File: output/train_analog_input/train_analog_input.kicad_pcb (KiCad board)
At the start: 2 copper layers, 65 x 40 mm, 29 parts, among them J1 Screw_Terminal_2P, J2 Screw_Terminal_2P, J3 Screw_Terminal_2P, J4 Screw_Terminal_2P, J5 PinHeader_1x04, U1 ADS1115

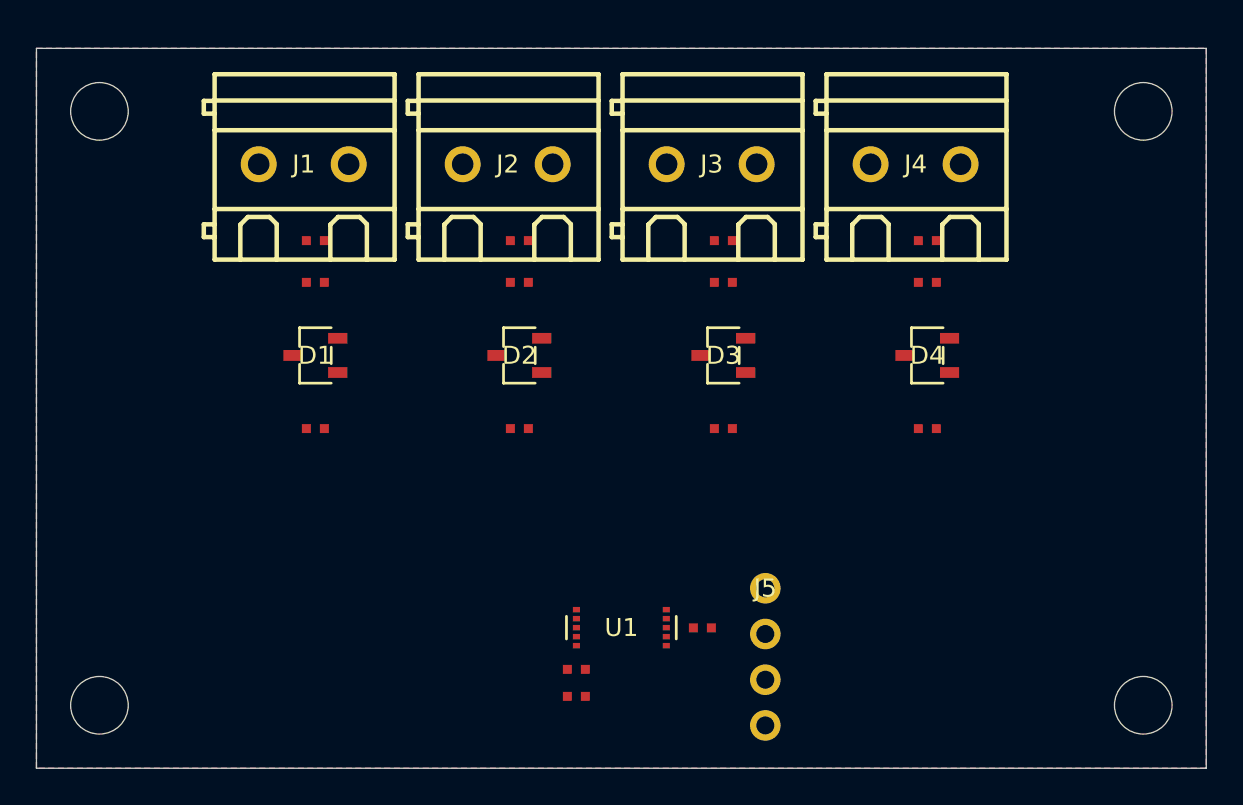
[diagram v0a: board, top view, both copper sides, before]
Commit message: pcb-review(analog): shift ADC components 2mm toward top edge
Moved J1-J4 and all ADC channel components (R1-R8, C2-C5, D1-D4)
2mm closer to the top board edge. Connector Edge score 0.871->0.940.
Score 0.9832 -> 0.9844. Grade A, 0 violations.

Co-Authored-By: Claude Opus 4.6 (1M context) <noreply@anthropic.com>
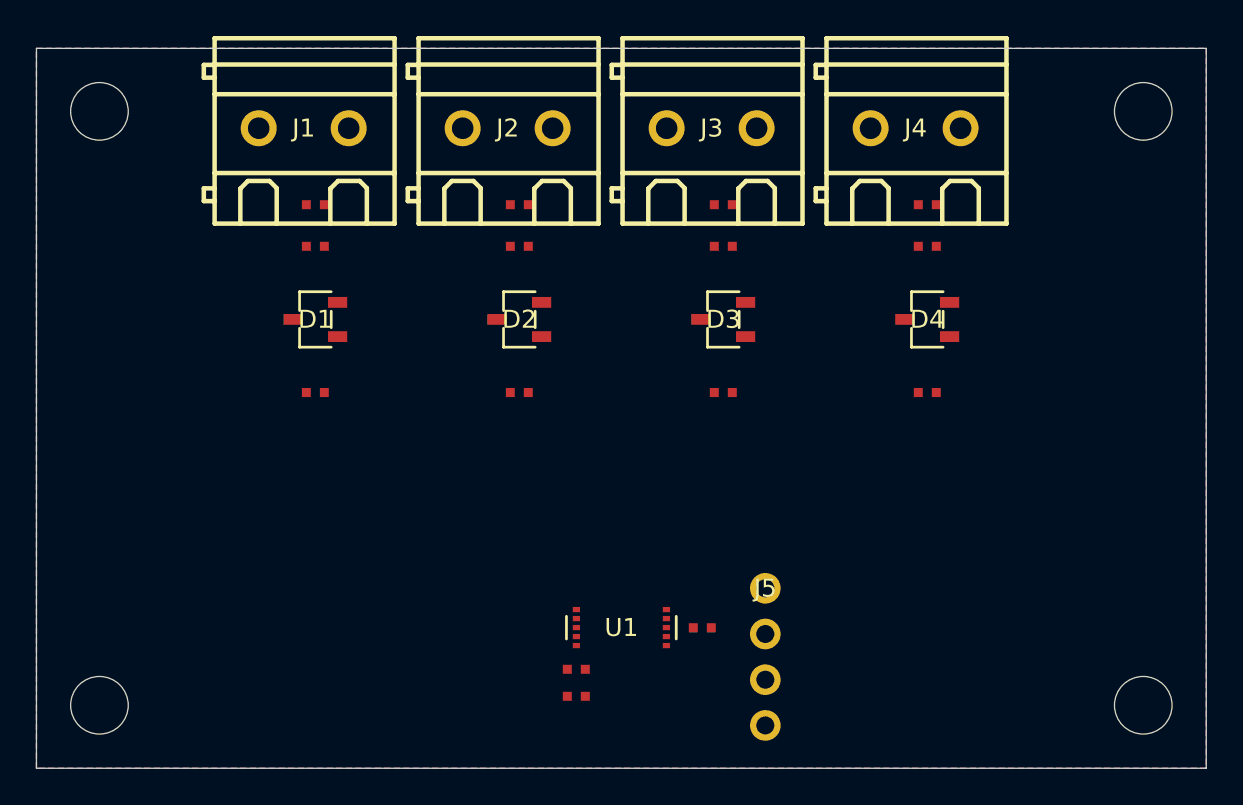
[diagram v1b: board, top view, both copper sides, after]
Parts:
- moved C2 2.00 mm to (15.5, 11.0)
- moved C3 2.00 mm to (26.8, 11.0)
- moved C4 2.00 mm to (38.2, 11.0)
- moved C5 2.00 mm to (49.5, 11.0)
- moved D1 2.00 mm to (15.5, 15.1)
- moved D2 2.00 mm to (26.8, 15.1)
- moved D3 2.00 mm to (38.2, 15.1)
- moved D4 2.00 mm to (49.5, 15.1)
- moved J1 2.00 mm to (14.8, 4.44)
- moved J2 2.00 mm to (26.2, 4.44)
- moved J3 2.00 mm to (37.5, 4.44)
- moved J4 2.00 mm to (48.9, 4.44)
- moved R1 2.00 mm to (15.5, 8.69)
- moved R2 2.00 mm to (15.5, 19.1)
- moved R3 2.00 mm to (26.8, 8.69)
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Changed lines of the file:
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@@
   (footprint "Resistor_SMD:R_0402_1005Metric"
     (layer "F.Cu")
-    (at 15.5 10.6875 0.0)
+    (at 15.5 8.6875 0.0)
     (attr smd)
     (property "Reference" "R1"
@@
   (footprint "Resistor_SMD:R_0402_1005Metric"
     (layer "F.Cu")
-    (at 15.5 21.125 0.0)
+    (at 15.5 19.125 0.0)
     (attr smd)
     (property "Reference" "R2"
@@
   (footprint "easyeda2kicad:SOT-23-3_L2.9-W1.6-P1.90-LS2.8-BR"
     (layer "F.Cu")
-    (at 15.5 17.0625 0.0)
+    (at 15.5 15.0625 0.0)
     (attr smd)
     (property "Reference" "D1"
@@
   (footprint "Capacitor_SMD:C_0402_1005Metric"
     (layer "F.Cu")
-    (at 15.5 13.0 0.0)
+    (at 15.5 11.0 0.0)
     (attr smd)
     (property "Reference" "C2"
@@
   (footprint "easyeda2kicad:CONN-TH_2P-P5.00_WJ128V-5.0-2P"
     (layer "F.Cu")
-    (at 14.85 6.4375 0.0)
+    (at 14.85 4.4375 0.0)
     (attr through_hole)
     (property "Reference" "J1"
@@
   (footprint "Resistor_SMD:R_0402_1005Metric"
     (layer "F.Cu")
-    (at 26.8333 10.6875 0.0)
+    (at 26.8333 8.6875 0.0)
     (attr smd)
     (property "Reference" "R3"
@@
   (footprint "Resistor_SMD:R_0402_1005Metric"
     (layer "F.Cu")
-    (at 26.8333 21.125 0.0)
+    (at 26.8333 19.125 0.0)
     (attr smd)
     (property "Reference" "R4"
@@
   (footprint "easyeda2kicad:SOT-23-3_L2.9-W1.6-P1.90-LS2.8-BR"
     (layer "F.Cu")
-    (at 26.8333 17.0625 0.0)
+    (at 26.8333 15.0625 0.0)
     (attr smd)
     (property "Reference" "D2"
@@
   (footprint "Capacitor_SMD:C_0402_1005Metric"
     (layer "F.Cu")
-    (at 26.8333 13.0 0.0)
+    (at 26.8333 11.0 0.0)
     (attr smd)
     (property "Reference" "C3"
@@
   (footprint "easyeda2kicad:CONN-TH_2P-P5.00_WJ128V-5.0-2P"
     (layer "F.Cu")
-    (at 26.1833 6.4375 0.0)
+    (at 26.1833 4.4375 0.0)
     (attr through_hole)
     (property "Reference" "J2"
@@
   (footprint "Resistor_SMD:R_0402_1005Metric"
     (layer "F.Cu")
-    (at 38.1667 10.6875 0.0)
+    (at 38.1667 8.6875 0.0)
     (attr smd)
     (property "Reference" "R5"
@@
   (footprint "Resistor_SMD:R_0402_1005Metric"
     (layer "F.Cu")
-    (at 38.1667 21.125 0.0)
+    (at 38.1667 19.125 0.0)
     (attr smd)
     (property "Reference" "R6"
@@
   (footprint "easyeda2kicad:SOT-23-3_L2.9-W1.6-P1.90-LS2.8-BR"
     (layer "F.Cu")
-    (at 38.1667 17.0625 0.0)
+    (at 38.1667 15.0625 0.0)
     (attr smd)
     (property "Reference" "D3"
@@
   (footprint "Capacitor_SMD:C_0402_1005Metric"
     (layer "F.Cu")
-    (at 38.1667 13.0 0.0)
+    (at 38.1667 11.0 0.0)
     (attr smd)
     (property "Reference" "C4"
@@
   (footprint "easyeda2kicad:CONN-TH_2P-P5.00_WJ128V-5.0-2P"
     (layer "F.Cu")
-    (at 37.5167 6.4375 0.0)
+    (at 37.5167 4.4375 0.0)
     (attr through_hole)
     (property "Reference" "J3"
@@
   (footprint "Resistor_SMD:R_0402_1005Metric"
     (layer "F.Cu")
-    (at 49.5 10.6875 0.0)
+    (at 49.5 8.6875 0.0)
     (attr smd)
     (property "Reference" "R7"
@@
   (footprint "Resistor_SMD:R_0402_1005Metric"
     (layer "F.Cu")
-    (at 49.5 21.125 0.0)
+    (at 49.5 19.125 0.0)
     (attr smd)
     (property "Reference" "R8"
@@
   (footprint "easyeda2kicad:SOT-23-3_L2.9-W1.6-P1.90-LS2.8-BR"
     (layer "F.Cu")
-    (at 49.5 17.0625 0.0)
+    (at 49.5 15.0625 0.0)
     (attr smd)
     (property "Reference" "D4"
@@
   (footprint "Capacitor_SMD:C_0402_1005Metric"
     (layer "F.Cu")
-    (at 49.5 13.0 0.0)
+    (at 49.5 11.0 0.0)
     (attr smd)
     (property "Reference" "C5"
@@
   (footprint "easyeda2kicad:CONN-TH_2P-P5.00_WJ128V-5.0-2P"
     (layer "F.Cu")
-    (at 48.85 6.4375 0.0)
+    (at 48.85 4.4375 0.0)
     (attr through_hole)
     (property "Reference" "J4"

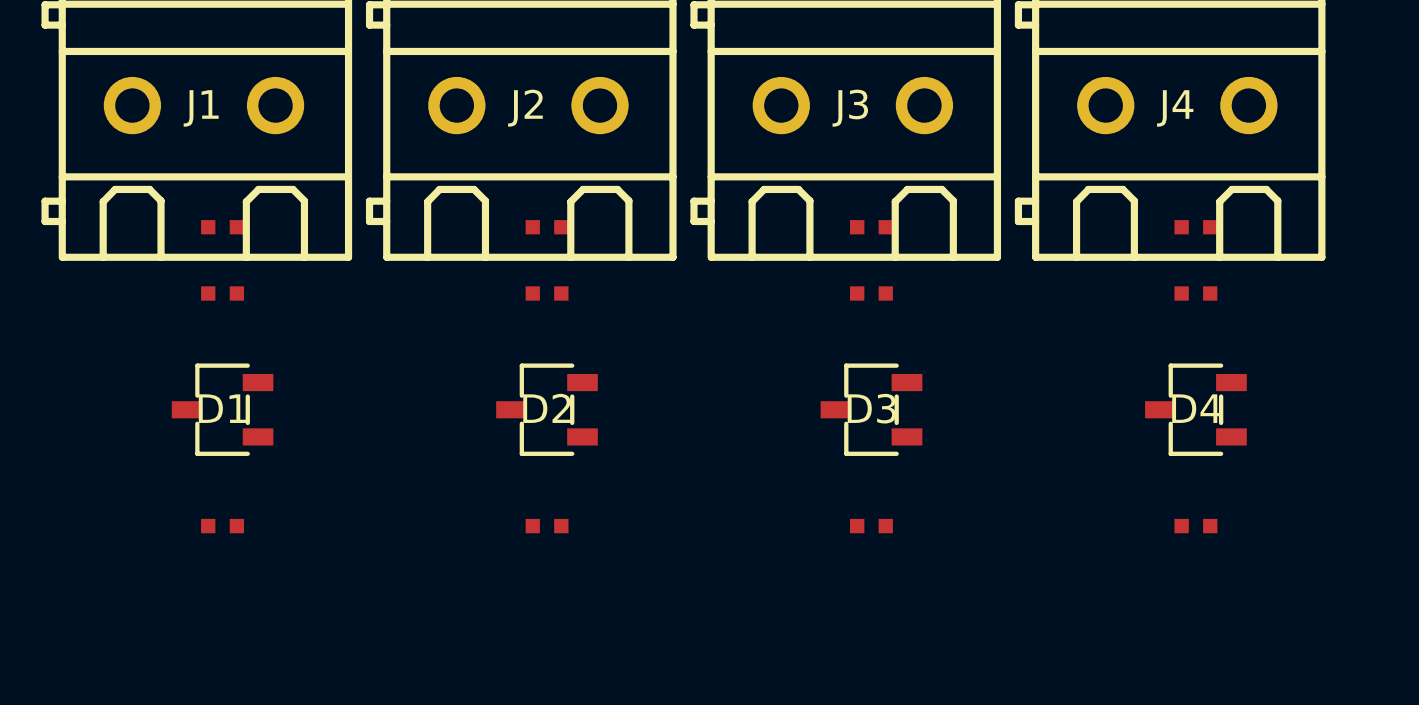
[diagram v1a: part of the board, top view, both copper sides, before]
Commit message: pcb-review(analog): compact ADC channel components vertically
Reduced spacing between R/C/D in each ADC channel (with proper
courtyard clearance for SOT-23 diodes). Subgroup cohesion now
passes (was 14.7mm spread, now <12mm).
Score 0.9844 -> 0.9856. Grade A, 0 violations.

Co-Authored-By: Claude Opus 4.6 (1M context) <noreply@anthropic.com>
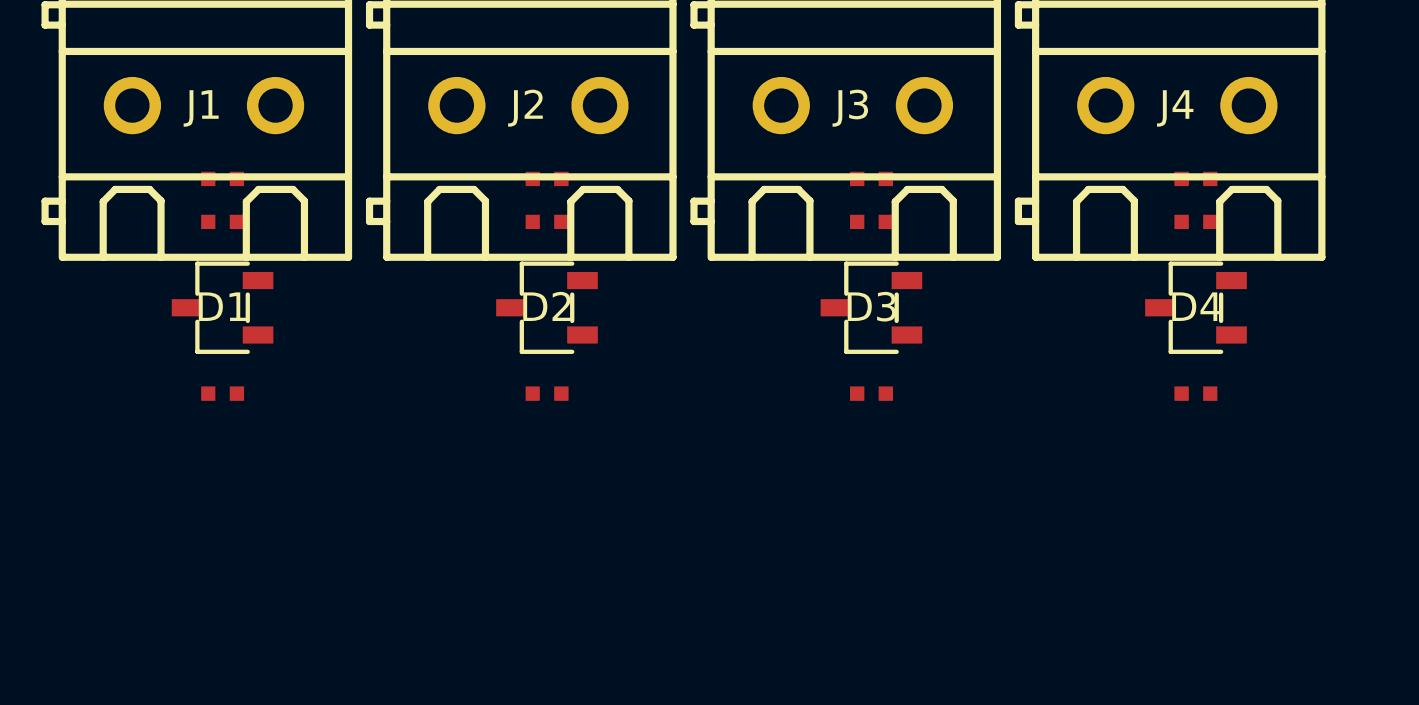
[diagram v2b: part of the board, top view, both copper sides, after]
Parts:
- moved R2 4.62 mm to (15.5, 14.5)
- moved R4 4.62 mm to (26.8, 14.5)
- moved R6 4.62 mm to (38.2, 14.5)
- moved R8 4.62 mm to (49.5, 14.5)
- moved D1 3.56 mm to (15.5, 11.5)
- moved D2 3.56 mm to (26.8, 11.5)
- moved D3 3.56 mm to (38.2, 11.5)
- moved D4 3.56 mm to (49.5, 11.5)
- moved C2 2.50 mm to (15.5, 8.50)
- moved C3 2.50 mm to (26.8, 8.50)
- moved C4 2.50 mm to (38.2, 8.50)
- moved C5 2.50 mm to (49.5, 8.50)
- moved R1 1.69 mm to (15.5, 7.00)
- moved R3 1.69 mm to (26.8, 7.00)
- moved R5 1.69 mm to (38.2, 7.00)
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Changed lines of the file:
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@@
   (footprint "Resistor_SMD:R_0402_1005Metric"
     (layer "F.Cu")
-    (at 15.5 8.6875 0.0)
+    (at 15.5 7.0 0.0)
     (attr smd)
     (property "Reference" "R1"
@@
   (footprint "Resistor_SMD:R_0402_1005Metric"
     (layer "F.Cu")
-    (at 15.5 19.125 0.0)
+    (at 15.5 14.5 0.0)
     (attr smd)
     (property "Reference" "R2"
@@
   (footprint "easyeda2kicad:SOT-23-3_L2.9-W1.6-P1.90-LS2.8-BR"
     (layer "F.Cu")
-    (at 15.5 15.0625 0.0)
+    (at 15.5 11.5 0.0)
     (attr smd)
     (property "Reference" "D1"
@@
   (footprint "Capacitor_SMD:C_0402_1005Metric"
     (layer "F.Cu")
-    (at 15.5 11.0 0.0)
+    (at 15.5 8.5 0.0)
     (attr smd)
     (property "Reference" "C2"
@@
   (footprint "Resistor_SMD:R_0402_1005Metric"
     (layer "F.Cu")
-    (at 26.8333 8.6875 0.0)
+    (at 26.8333 7.0 0.0)
     (attr smd)
     (property "Reference" "R3"
@@
   (footprint "Resistor_SMD:R_0402_1005Metric"
     (layer "F.Cu")
-    (at 26.8333 19.125 0.0)
+    (at 26.8333 14.5 0.0)
     (attr smd)
     (property "Reference" "R4"
@@
   (footprint "easyeda2kicad:SOT-23-3_L2.9-W1.6-P1.90-LS2.8-BR"
     (layer "F.Cu")
-    (at 26.8333 15.0625 0.0)
+    (at 26.8333 11.5 0.0)
     (attr smd)
     (property "Reference" "D2"
@@
   (footprint "Capacitor_SMD:C_0402_1005Metric"
     (layer "F.Cu")
-    (at 26.8333 11.0 0.0)
+    (at 26.8333 8.5 0.0)
     (attr smd)
     (property "Reference" "C3"
@@
   (footprint "Resistor_SMD:R_0402_1005Metric"
     (layer "F.Cu")
-    (at 38.1667 8.6875 0.0)
+    (at 38.1667 7.0 0.0)
     (attr smd)
     (property "Reference" "R5"
@@
   (footprint "Resistor_SMD:R_0402_1005Metric"
     (layer "F.Cu")
-    (at 38.1667 19.125 0.0)
+    (at 38.1667 14.5 0.0)
     (attr smd)
     (property "Reference" "R6"
@@
   (footprint "easyeda2kicad:SOT-23-3_L2.9-W1.6-P1.90-LS2.8-BR"
     (layer "F.Cu")
-    (at 38.1667 15.0625 0.0)
+    (at 38.1667 11.5 0.0)
     (attr smd)
     (property "Reference" "D3"
@@
   (footprint "Capacitor_SMD:C_0402_1005Metric"
     (layer "F.Cu")
-    (at 38.1667 11.0 0.0)
+    (at 38.1667 8.5 0.0)
     (attr smd)
     (property "Reference" "C4"
@@
   (footprint "Resistor_SMD:R_0402_1005Metric"
     (layer "F.Cu")
-    (at 49.5 8.6875 0.0)
+    (at 49.5 7.0 0.0)
     (attr smd)
     (property "Reference" "R7"
@@
   (footprint "Resistor_SMD:R_0402_1005Metric"
     (layer "F.Cu")
-    (at 49.5 19.125 0.0)
+    (at 49.5 14.5 0.0)
     (attr smd)
     (property "Reference" "R8"
@@
   (footprint "easyeda2kicad:SOT-23-3_L2.9-W1.6-P1.90-LS2.8-BR"
     (layer "F.Cu")
-    (at 49.5 15.0625 0.0)
+    (at 49.5 11.5 0.0)
     (attr smd)
     (property "Reference" "D4"
@@
   (footprint "Capacitor_SMD:C_0402_1005Metric"
     (layer "F.Cu")
-    (at 49.5 11.0 0.0)
+    (at 49.5 8.5 0.0)
     (attr smd)
     (property "Reference" "C5"

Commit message: pcb-review(analog): rotate R1-R8 90deg for signal flow alignment
Rotated ADC channel resistors to face N/S matching vertical signal
flow (connectors at top -> U1 at bottom). Pad facing score improved
from 0.500 to 0.803.
Score 0.9856 -> 0.9882. Grade A, 0 violations.

Co-Authored-By: Claude Opus 4.6 (1M context) <noreply@anthropic.com>
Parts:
- turned R1 to 90 degrees
- turned R2 to 90 degrees
- turned R3 to 90 degrees
- turned R4 to 90 degrees
- turned R5 to 90 degrees
- turned R6 to 90 degrees
- turned R7 to 90 degrees
- turned R8 to 90 degrees
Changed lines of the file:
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@@
   (footprint "Resistor_SMD:R_0402_1005Metric"
     (layer "F.Cu")
-    (at 15.5 7.0 0.0)
+    (at 15.5 7.0 90.0)
     (attr smd)
     (property "Reference" "R1"
@@
   (footprint "Resistor_SMD:R_0402_1005Metric"
     (layer "F.Cu")
-    (at 15.5 14.5 0.0)
+    (at 15.5 14.5 90.0)
     (attr smd)
     (property "Reference" "R2"
@@
   (footprint "Resistor_SMD:R_0402_1005Metric"
     (layer "F.Cu")
-    (at 26.8333 7.0 0.0)
+    (at 26.8333 7.0 90.0)
     (attr smd)
     (property "Reference" "R3"
@@
   (footprint "Resistor_SMD:R_0402_1005Metric"
     (layer "F.Cu")
-    (at 26.8333 14.5 0.0)
+    (at 26.8333 14.5 90.0)
     (attr smd)
     (property "Reference" "R4"
@@
   (footprint "Resistor_SMD:R_0402_1005Metric"
     (layer "F.Cu")
-    (at 38.1667 7.0 0.0)
+    (at 38.1667 7.0 90.0)
     (attr smd)
     (property "Reference" "R5"
@@
   (footprint "Resistor_SMD:R_0402_1005Metric"
     (layer "F.Cu")
-    (at 38.1667 14.5 0.0)
+    (at 38.1667 14.5 90.0)
     (attr smd)
     (property "Reference" "R6"
@@
   (footprint "Resistor_SMD:R_0402_1005Metric"
     (layer "F.Cu")
-    (at 49.5 7.0 0.0)
+    (at 49.5 7.0 90.0)
     (attr smd)
     (property "Reference" "R7"
@@
   (footprint "Resistor_SMD:R_0402_1005Metric"
     (layer "F.Cu")
-    (at 49.5 14.5 0.0)
+    (at 49.5 14.5 90.0)
     (attr smd)
     (property "Reference" "R8"
